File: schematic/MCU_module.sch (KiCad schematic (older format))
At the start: 49 parts

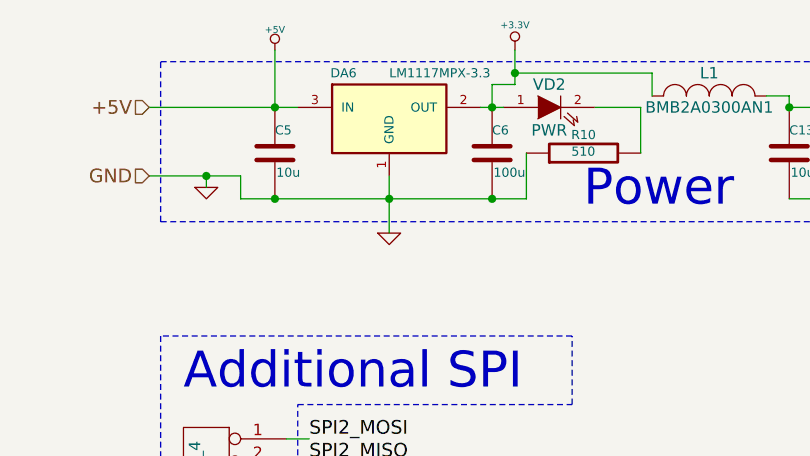
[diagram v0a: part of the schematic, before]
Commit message: Shutter module tested
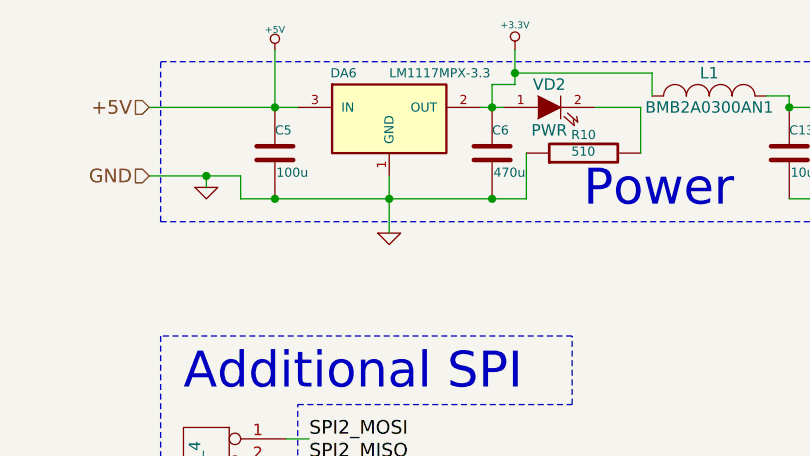
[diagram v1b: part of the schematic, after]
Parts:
- C5: value 10u -> 100u
- C6: value 100u -> 470u
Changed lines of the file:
@@
-EESchema Schematic File Version 2  date Ср 28 янв 2015 08:47:22
+EESchema Schematic File Version 2  date Ср 04 фев 2015 15:06:53
 LIBS:power
 LIBS:device
@@
 Sheet 3 12
 Title "MCU module on STM32F103"
-Date "28 jan 2015"
+Date "4 feb 2015"
 Rev ""
 Comp "SAO RAS"
@@
 P 4400 1100
 F 0 "C5" H 4400 1200 40  0000 L CNN
-F 1 "10u" H 4406 1015 40  0000 L CNN
+F 1 "100u" H 4406 1015 40  0000 L CNN
 F 2 "C2" H 4438 950 30  0001 C CNN
 F 3 "~" H 4400 1100 60  0000 C CNN
@@
 P 5350 1100
 F 0 "C6" H 5350 1200 40  0000 L CNN
-F 1 "100u" H 5356 1015 40  0000 L CNN
+F 1 "470u" H 5356 1015 40  0000 L CNN
 F 2 "C2" H 5388 950 30  0001 C CNN
 F 3 "~" H 5350 1100 60  0000 C CNN

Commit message: Fixed bugs when work in mustdie's terminal
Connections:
- net labels added: Tur3_3
- net labels removed: Tur1_3
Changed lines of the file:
@@
-EESchema Schematic File Version 2  date Ср 04 фев 2015 15:06:53
+EESchema Schematic File Version 2  date Чт 02 апр 2015 10:40:58
 LIBS:power
 LIBS:device
@@
 Sheet 3 12
 Title "MCU module on STM32F103"
-Date "4 feb 2015"
+Date "2 apr 2015"
 Rev ""
 Comp "SAO RAS"
@@
 Hall[0..9]
 NoConn ~ 12600 4100
+Text Label 11800 4100 1    61   ~ 0
+Tur3_1
 Text Label 11400 4100 1    61   ~ 0
-Tur3_1
-Text Label 11300 4100 1    61   ~ 0
 Tur3_2
 Text Label 12500 4100 1    61   ~ 0
@@
 Tur1_2
 Text Label 12200 4100 1    61   ~ 0
-Tur1_3
+Tur2_0
 Text Label 12100 4100 1    61   ~ 0
-Tur2_0
+Tur2_1
 Text Label 12000 4100 1    61   ~ 0
-Tur2_1
+Tur2_2
 Text Label 11900 4100 1    61   ~ 0
-Tur2_2
-Text Label 11800 4100 1    61   ~ 0
 Tur3_0
 Entry Wire Line
@@
 	1800 7500 1900 7600
 Entry Wire Line
-	1800 7650 1900 7750
+	1800 7800 1900 7900
 Entry Wire Line
 	1800 7950 1900 8050
@@
 	1800 8100 1900 8200
 Entry Wire Line
-	1800 8250 1900 8350
+	1800 8400 1900 8500
 Entry Wire Line
 	1800 8550 1900 8650
@@
 Text Label 2000 7600 0    61   ~ 0
 Hall2
-Text Label 2000 7750 0    61   ~ 0
+Text Label 2000 7900 0    61   ~ 0
 Hall3
 Text Label 2000 8050 0    61   ~ 0
@@
 Text Label 2000 8200 0    61   ~ 0
 Hall5
-Text Label 2000 8350 0    61   ~ 0
+Text Label 2000 8500 0    61   ~ 0
 Hall6
 Text Label 2000 8650 0    61   ~ 0
@@
 Text Label 2500 7600 0    61   ~ 0
 Tur1_2
-Text Label 2500 7750 0    61   ~ 0
-Tur1_3
+Text Label 2500 7900 0    61   ~ 0
+Tur2_0
 Text Label 2500 8050 0    61   ~ 0
-Tur2_0
+Tur2_1
 Text Label 2500 8200 0    61   ~ 0
-Tur2_1
-Text Label 2500 8350 0    61   ~ 0
 Tur2_2
+Text Label 2500 8500 0    61   ~ 0
+Tur3_0
 Text Label 2500 8650 0    61   ~ 0
-Tur3_0
+Tur3_1
 Text Label 2500 8800 0    61   ~ 0
-Tur3_1
-Text Label 2500 8950 0    61   ~ 0
 Tur3_2
 $Comp
@@
 	1900 7600 2500 7600
 Wire Wire Line
-	1900 7750 2500 7750
+	1900 7900 2500 7900
 Wire Wire Line
 	1900 8050 2500 8050
@@
 	1900 8200 2500 8200
 Wire Wire Line
-	1900 8350 2500 8350
+	1900 8500 2500 8500
 Wire Wire Line
 	1900 8650 2500 8650
@@
 Text Label 8300 7600 2    60   ~ 0
 U10_ADC
+Text Label 2500 8950 0    61   ~ 0
+Tur3_3
+Text Label 11300 4100 1    61   ~ 0
+Tur3_3
 $EndSCHEMATC
